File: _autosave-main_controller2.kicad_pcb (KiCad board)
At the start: 4 copper layers, 55.1 x 55.1 mm, 71 parts, among them J1 xt30, J10 Conn_01x15, J3 xt30, J4 Conn_01x02, J6 Conn_01x02, J7 Conn_01x02, J8 Conn_01x02, J9 Conn_01x16, Q1 FDN359BN, SW1 SW_SPST, SW2 SW_SPST, U1 ESP32-PICO-MINI-02, U10 BTN7030-1EPA, U11 PCA9557PW, U13 W25N02KVZEIR, U14 MCP2517FD-xSL, U15 SN65HVD230, U2 BMI088, U3 china_buck_converter, U4 AP7361-33ER-13, U5 MS5611-01BA, U6 BTS70802, U7 BTN7030-1EPA, U8 BTN7030-1EPA, U9 BTN7030-1EPA, Y1 40MHz

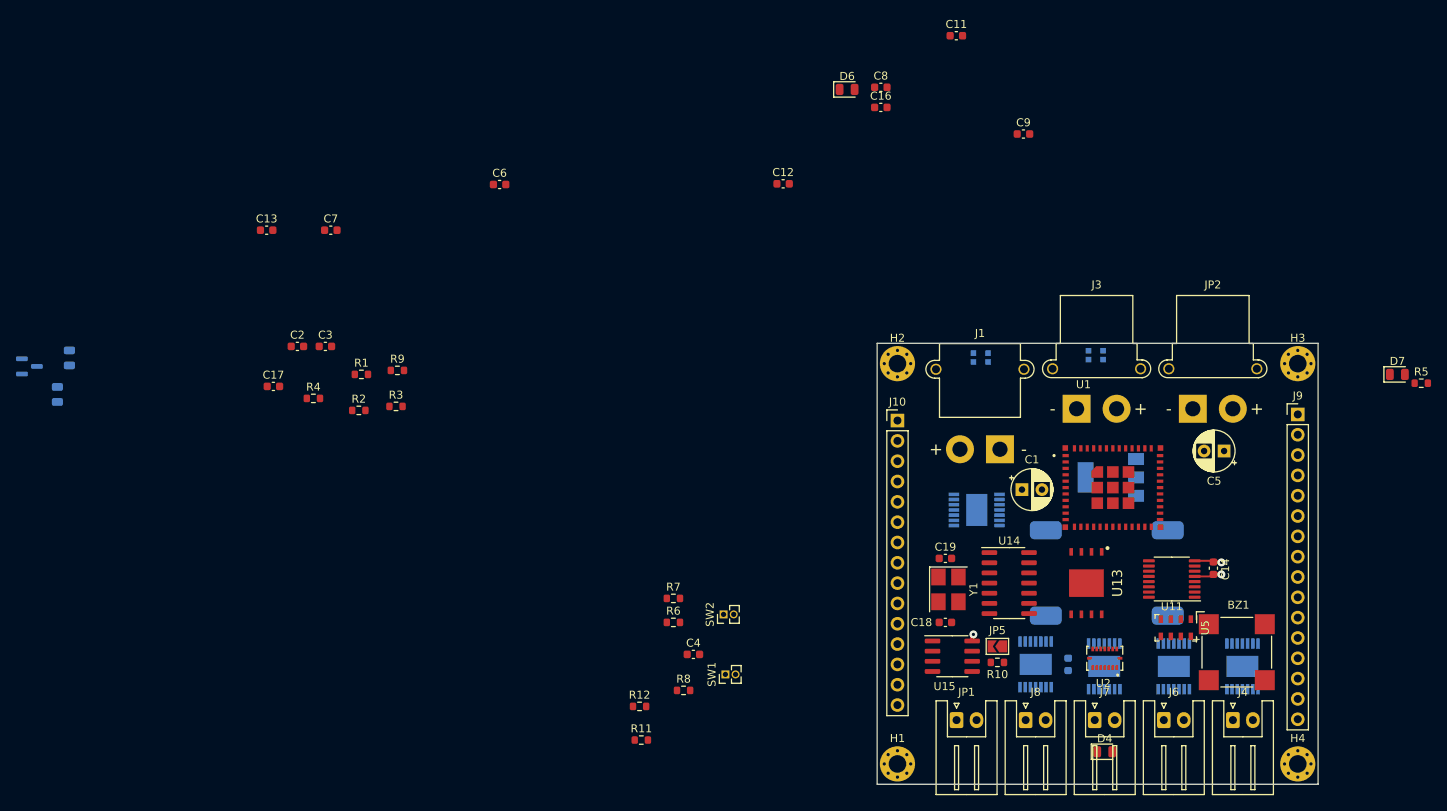
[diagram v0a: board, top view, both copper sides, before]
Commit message: Placing all components, far from finished, basic routing started
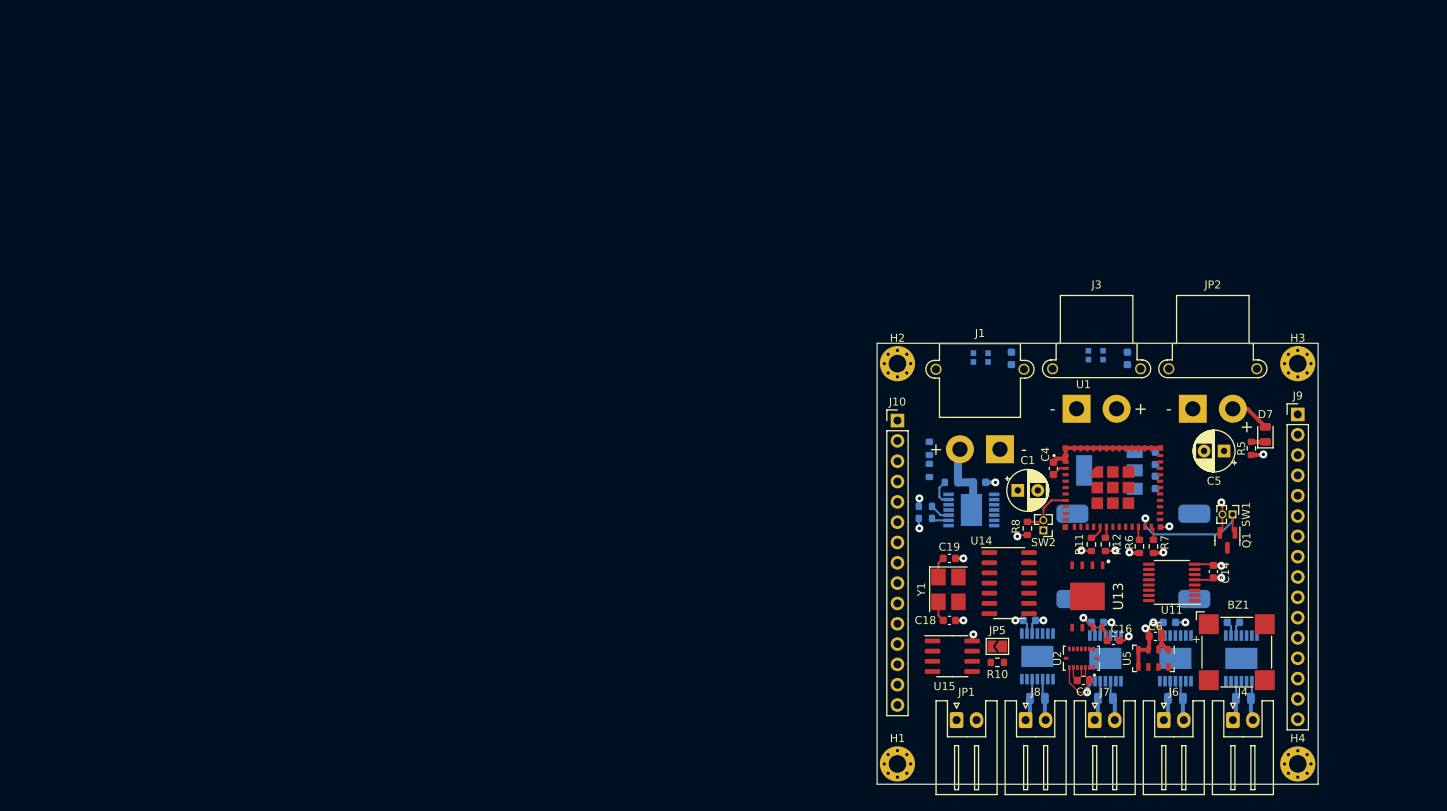
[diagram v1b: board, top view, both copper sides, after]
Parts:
- C11, C12, C13, C17, C2, C3, C8, C9, D4, D6, R1, R2, R3, R4, R9: moved to B.Cu
- Q1: moved to F.Cu
- moved D3 152.8 mm to (239.1, 142.7), turned to 0 degrees
- moved Q1 151.3 mm to (237.1, 123.0), turned to -90 degrees
- moved D5 144.8 mm to (230.6, 142.7), turned to 0 degrees
- moved C7 109.6 mm to (219.1, 140.5), turned to 180 degrees
- moved C2 108.2 mm to (228.1, 112.7), turned to 90 degrees
- moved C13 107.1 mm to (212.4, 133.0)
- moved C3 105.1 mm to (228.1, 115.7), turned to -90 degrees
- moved C6 99.5 mm to (228.1, 135.0), turned to 180 degrees
- moved C17 89.1 mm to (206.1, 115.7)
- moved R4 80.4 mm to (202.6, 115.7), turned to 180 degrees
- moved D6 79.7 mm to (213.4, 142.7)
- moved C11 78.0 mm to (229.9, 133.2)
- moved C16 72.7 mm to (222.9, 135.5)
- moved R2 71.7 mm to (199.9, 114.2), turned to -90 degrees
- moved R1 71.6 mm to (199.9, 111.5), turned to -90 degrees
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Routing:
- net Earth: track 4.31 -> 72.6 mm, vias 2 -> 15
- net +3V3: track 3.44 -> 38.8 mm, vias 1 -> 10
- net /BOOTLOADER: track 0.00 -> 17.3 mm, vias 0 -> 1
- net +BATT: track 0.00 -> 9.68 mm
- net Net-(R8-Pad2): track 0.00 -> 6.76 mm
- net /PYRO_4: track 0.00 -> 5.27 mm
- net /PYRO_3: track 0.00 -> 5.07 mm
- net /EDDA_PWR: track 0.00 -> 5.03 mm
- net /PYRO_2: track 0.00 -> 5.03 mm
- net /PYRO_1: track 0.00 -> 5.01 mm
- net Net-(JP1-Pad2): track 0.00 -> 3.39 mm
- net Net-(C18-Pad1): track 0.00 -> 2.57 mm
- net Net-(C19-Pad1): track 0.00 -> 2.57 mm
- net /CURR_EN: track 0.00 -> 2.53 mm
- net /EDDA_EN: track 0.00 -> 2.18 mm
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- added copper zone on In2.Cu, net Earth
- removed copper zone on In2.Cu, net /GND
